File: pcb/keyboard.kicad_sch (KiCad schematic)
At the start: 50 parts, among them J1 TRRS, SW11 11, SW12 12, SW13 13, SW14 14, SW15 15, SW16 16, SW17 17, SW18 18, SW19 19, SW21 21, SW22 22, SW23 23, SW24 24, SW25 25, SW26 26, SW27 27, SW28 28, SW29 29, SW31 31, SW32 32, SW33 33, SW34 34, SW35 35, SW36 36, SW37 37, SW38 38, SW39 39, SW41 41, SW42 42, SW43 43, SW45 45, SW46 46, SW47 47, SW48 48, SW49 49, U1 EliteC

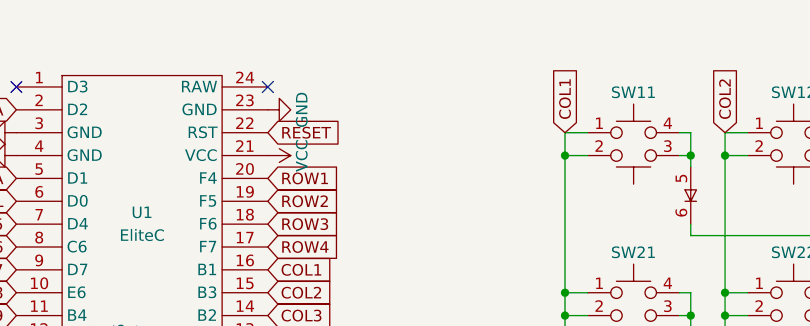
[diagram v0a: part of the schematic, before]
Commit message: add plate to 3D view
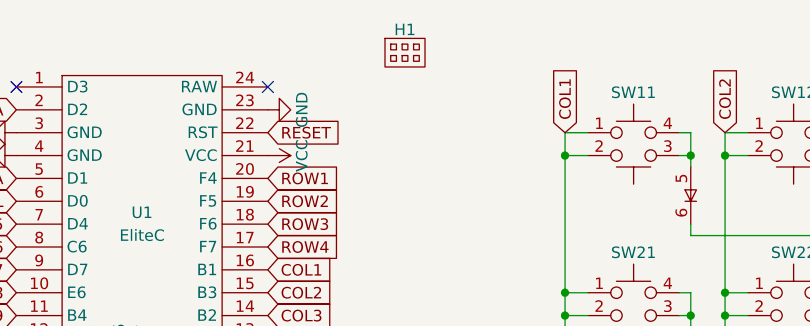
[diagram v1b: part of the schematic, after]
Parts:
- added H1: H1, Keyboard:RightPlate, symbol Keyboard:Plate
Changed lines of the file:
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@@
+    )
+  )
+  (symbol (lib_id "Keyboard:Plate") (at 85.09 30.48 0) (unit 1)
+    (in_bom yes) (on_board yes) (dnp no) (fields_autoplaced)
+    (property "Reference" "H1" (at 85.09 27.94 0) (do_not_autoplace)
+      (effects (font (size 1.27 1.27)))
+    )
+    (property "Value" "H1" (at 84.1375 30.1625 0) (do_not_autoplace)
+      (effects (font (size 1.27 1.27)) hide)
+    )
+    (property "Footprint" "Keyboard:RightPlate" (at 84.1375 30.1625 0)
+      (effects (font (size 1.27 1.27)) hide)
+    )
+    (property "Datasheet" "" (at 84.1375 30.1625 0)
+      (effects (font (size 1.27 1.27)) hide)
+    )
+    (instances
+      (project "keyboard"
+        (path "/7807834d-3d77-4d25-b9d8-d933072c7b84"
+          (reference "H1") (unit 1)
+        )
+      )
     )
   )

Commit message: move graphical copper arcs to traces; use default teardrop size
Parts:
- SW37, SW39: footprint Keyboard:Switch -> Keyboard:SwitchNo3D
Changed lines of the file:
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@@
       (effects (font (size 1.27 1.27)) hide)
     )
-    (property "Footprint" "Keyboard:Switch" (at 217.17 76.2 0)
+    (property "Footprint" "Keyboard:SwitchNo3D" (at 217.17 76.2 0)
       (effects (font (size 1.27 1.27)) hide)
     )
@@
       (effects (font (size 1.27 1.27)) hide)
     )
-    (property "Footprint" "Keyboard:Switch" (at 252.73 76.2 0)
-      (effects (font (size 1.27 1.27)) hide)
-    )
+    (property "Footprint" "Keyboard:SwitchNo3D" (at 252.73 76.2 0)
+      (effects (font (size 1.27 1.27)) hide)
+    )

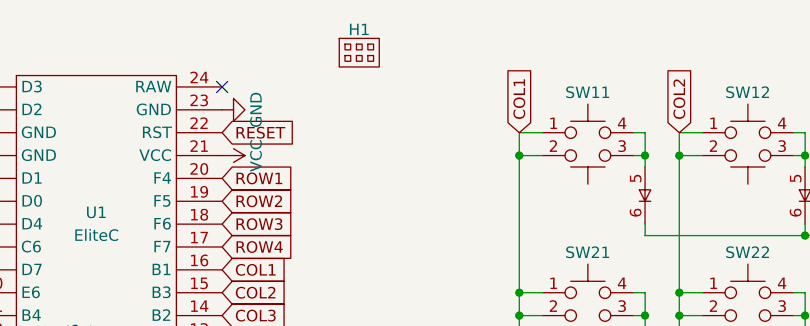
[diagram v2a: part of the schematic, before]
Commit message: support 3d view of left plate
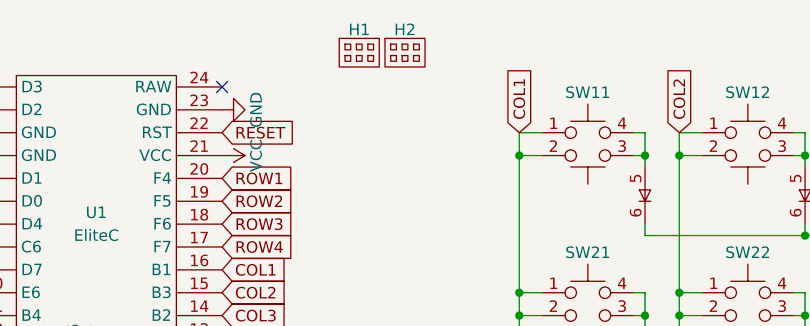
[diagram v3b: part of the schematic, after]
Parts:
- added H2: H1, Keyboard:LeftPlate, symbol Keyboard:Plate
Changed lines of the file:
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@@
+    )
+  )
+  (symbol (lib_id "Keyboard:Plate") (at 90.17 30.48 0) (unit 1)
+    (in_bom yes) (on_board yes) (dnp no) (fields_autoplaced)
+    (property "Reference" "H2" (at 90.17 27.94 0) (do_not_autoplace)
+      (effects (font (size 1.27 1.27)))
+    )
+    (property "Value" "H1" (at 89.2175 30.1625 0) (do_not_autoplace)
+      (effects (font (size 1.27 1.27)) hide)
+    )
+    (property "Footprint" "Keyboard:LeftPlate" (at 89.2175 30.1625 0)
+      (effects (font (size 1.27 1.27)) hide)
+    )
+    (property "Datasheet" "" (at 89.2175 30.1625 0)
+      (effects (font (size 1.27 1.27)) hide)
+    )
+    (instances
+      (project "keyboard"
+        (path "/7807834d-3d77-4d25-b9d8-d933072c7b84"
+          (reference "H2") (unit 1)
+        )
+      )
     )
   )

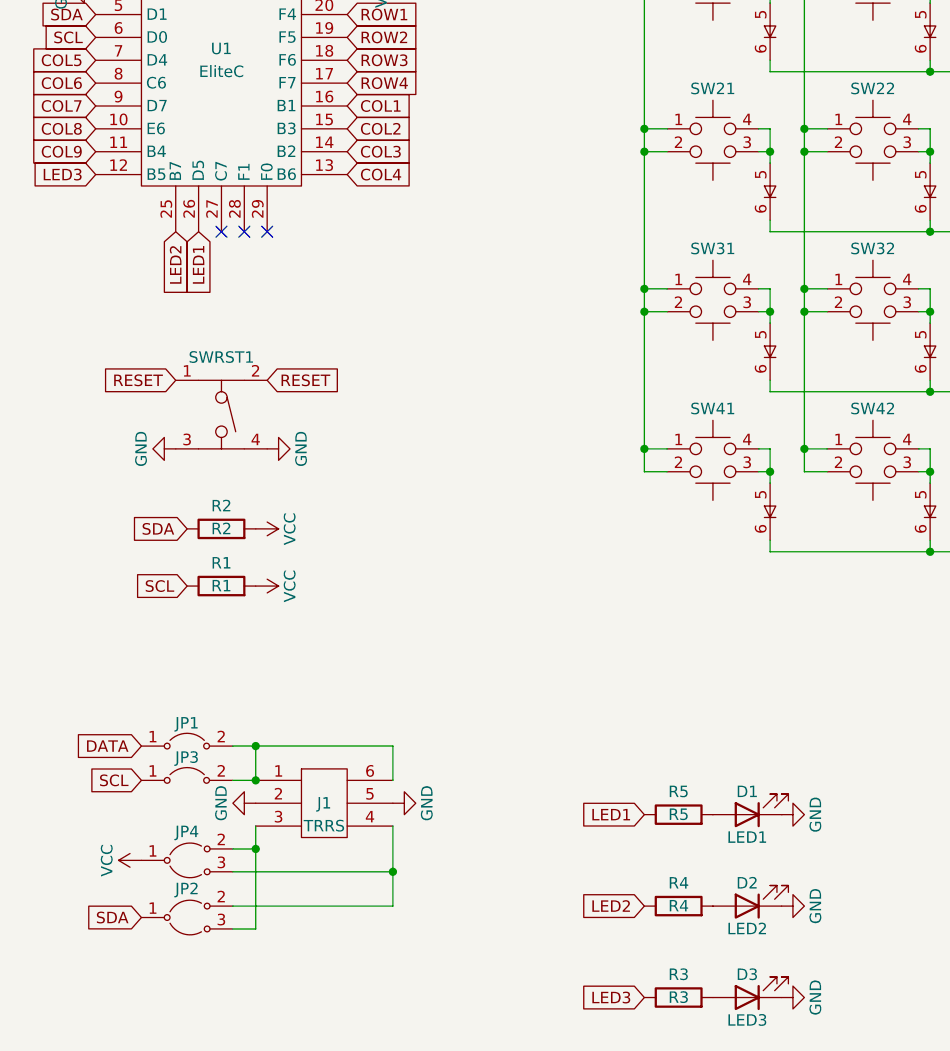
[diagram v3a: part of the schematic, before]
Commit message: hide back of LED by rotation; resistor after LED
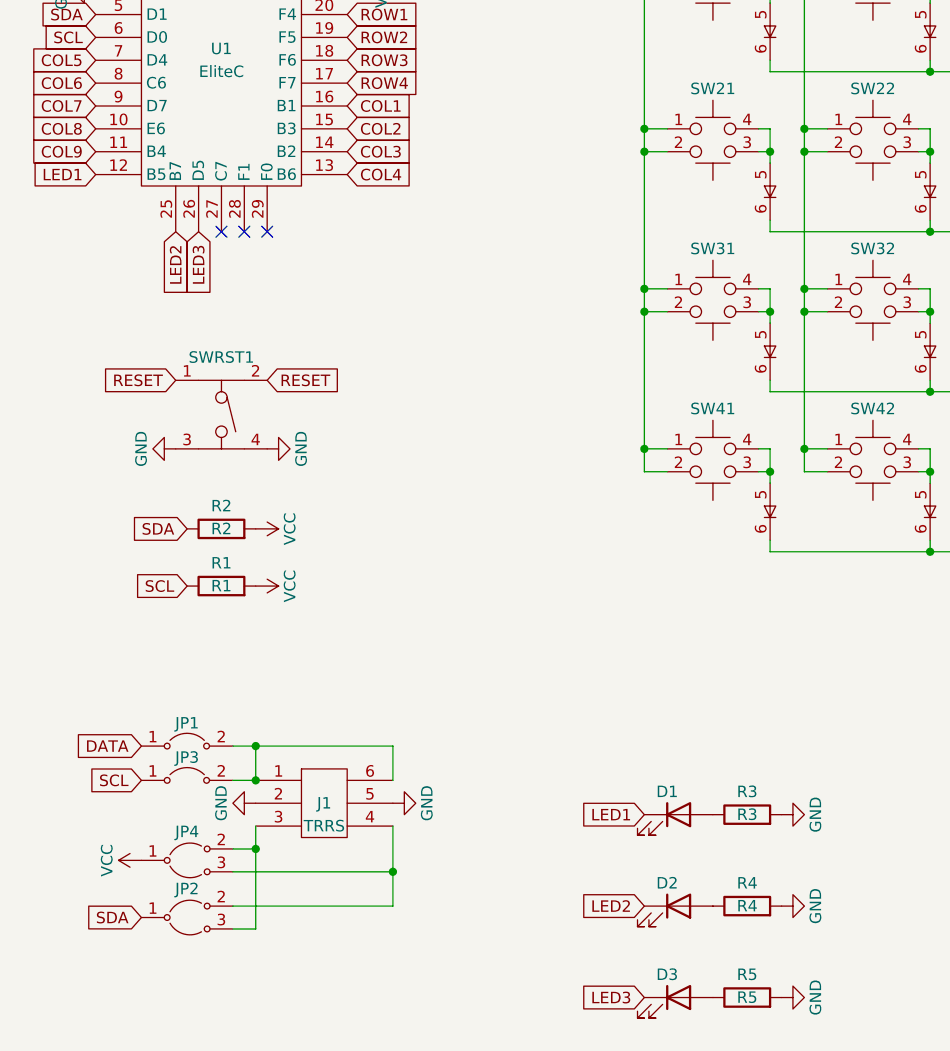
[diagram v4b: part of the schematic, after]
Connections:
- net GND: now also R3.2, R4.2, R5.2; no longer D1.1 (K), D2.1 (K), D3.1 (K)
- net LED1: now also D1.1 (K), U1.12 (B5); no longer R5.1, U1.26 (D5)
- net LED2: now also D2.1 (K); no longer R4.1
- net LED3: now also D3.1 (K), U1.26 (D5); no longer R3.1, U1.12 (B5)
- net at D3.2 (A): now also R5.1; no longer R3.2
- net at D1.2 (A): now also R3.1; no longer R5.2
- net at D2.2 (A): now also R4.1; no longer R4.2

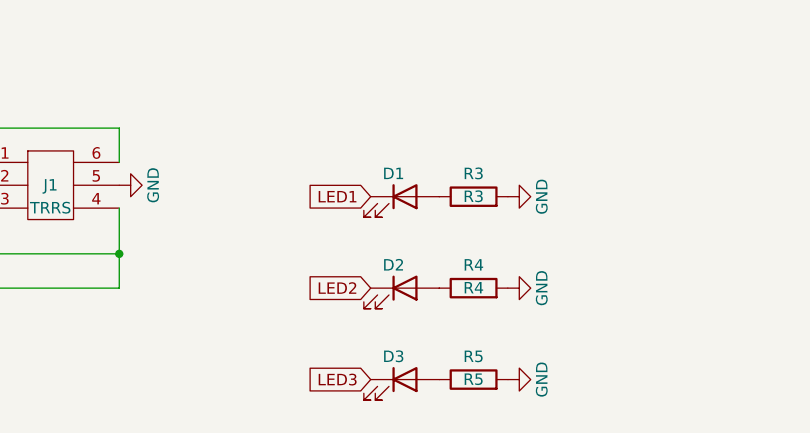
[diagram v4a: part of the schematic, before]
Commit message: fix schematic of LED pins
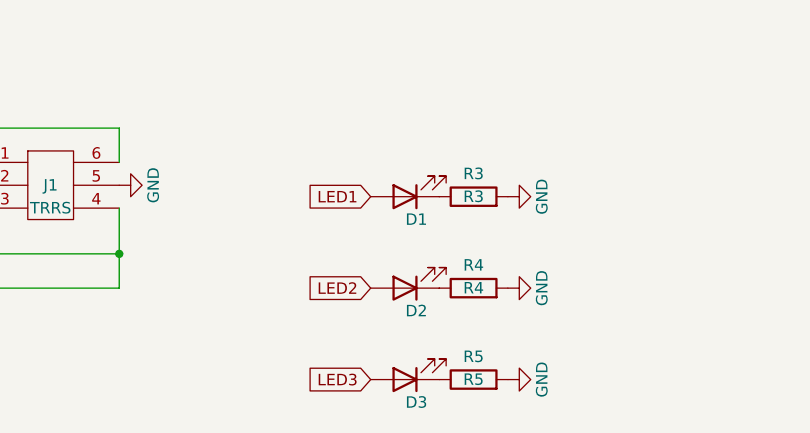
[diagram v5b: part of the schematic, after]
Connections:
- net LED1: now also D1.2 (A); no longer D1.1 (K)
- net LED2: now also D2.2 (A); no longer D2.1 (K)
- net LED3: now also D3.2 (A); no longer D3.1 (K)
- net at R5.1: now also D3.1 (K); no longer D3.2 (A)
- net at R4.1: now also D2.1 (K); no longer D2.2 (A)
- net at R3.1: now also D1.1 (K); no longer D1.2 (A)
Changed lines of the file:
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@@
-    )
-  )
-  (symbol (lib_id "Device:LED") (at 106.68 153.67 0) (unit 1)
-    (in_bom yes) (on_board yes) (dnp no)
-    (property "Reference" "D3" (at 105.41 151.13 0)
-      (effects (font (size 1.27 1.27)))
-    )
-    (property "Value" "LED3" (at 105.0925 149.86 0)
-      (effects (font (size 1.27 1.27)) hide)
-    )
-    (property "Footprint" "Keyboard:LED" (at 106.68 153.67 0)
-      (effects (font (size 1.27 1.27)) hide)
-    )
-    (property "Datasheet" "~" (at 106.68 153.67 0)
-      (effects (font (size 1.27 1.27)) hide)
-    )
-    (pin "1")
-    (pin "2")
-    (instances
-      (project "keyboard"
-        (path "/7807834d-3d77-4d25-b9d8-d933072c7b84"
-          (reference "D3") (unit 1)
-        )
-      )
     )
   )
@@
     )
   )
-  (symbol (lib_id "Device:LED") (at 106.68 143.51 0) (unit 1)
-    (in_bom yes) (on_board yes) (dnp no)
-    (property "Reference" "D2" (at 105.41 140.97 0)
-      (effects (font (size 1.27 1.27)))
-    )
-    (property "Value" "LED2" (at 105.0925 139.7 0)
-      (effects (font (size 1.27 1.27)) hide)
-    )
-    (property "Footprint" "Keyboard:LED" (at 106.68 143.51 0)
-      (effects (font (size 1.27 1.27)) hide)
-    )
-    (property "Datasheet" "~" (at 106.68 143.51 0)
-      (effects (font (size 1.27 1.27)) hide)
-    )
-    (pin "1")
-    (pin "2")
-    (instances
-      (project "keyboard"
-        (path "/7807834d-3d77-4d25-b9d8-d933072c7b84"
-          (reference "D2") (unit 1)
-        )
-      )
-    )
-  )
   (symbol (lib_id "Keyboard:Switch") (at 163.83 76.2 0) (unit 1)
     (in_bom yes) (on_board yes) (dnp no) (fields_autoplaced)
@@
     )
   )
+  (symbol (lib_id "Device:LED") (at 106.68 143.51 180) (unit 1)
+    (in_bom yes) (on_board yes) (dnp no)
+    (property "Reference" "D2" (at 107.95 146.05 0)
+      (effects (font (size 1.27 1.27)))
+    )
+    (property "Value" "LED2" (at 108.2675 147.32 0)
+      (effects (font (size 1.27 1.27)) hide)
+    )
+    (property "Footprint" "Keyboard:LED" (at 106.68 143.51 0)
+      (effects (font (size 1.27 1.27)) hide)
+    )
+    (property "Datasheet" "~" (at 106.68 143.51 0)
+      (effects (font (size 1.27 1.27)) hide)
+    )
+    (pin "1")
+    (pin "2")
+    (instances
+      (project "keyboard"
+        (path "/7807834d-3d77-4d25-b9d8-d933072c7b84"
+          (reference "D2") (unit 1)
+        )
+      )
+    )
+  )
   (symbol (lib_id "Keyboard:Switch") (at 217.17 40.64 0) (unit 1)
     (in_bom yes) (on_board yes) (dnp no) (fields_autoplaced)
@@
     )
   )
+  (symbol (lib_id "Device:LED") (at 106.68 153.67 180) (unit 1)
+    (in_bom yes) (on_board yes) (dnp no)
+    (property "Reference" "D3" (at 107.95 156.21 0)
+      (effects (font (size 1.27 1.27)))
+    )
+    (property "Value" "LED3" (at 108.2675 157.48 0)
+      (effects (font (size 1.27 1.27)) hide)
+    )
+    (property "Footprint" "Keyboard:LED" (at 106.68 153.67 0)
+      (effects (font (size 1.27 1.27)) hide)
+    )
+    (property "Datasheet" "~" (at 106.68 153.67 0)
+      (effects (font (size 1.27 1.27)) hide)
+    )
+    (pin "1")
+    (pin "2")
+    (instances
+      (project "keyboard"
+        (path "/7807834d-3d77-4d25-b9d8-d933072c7b84"
+          (reference "D3") (unit 1)
+        )
+      )
+    )
+  )
   (symbol (lib_id "power:VCC") (at 69.85 41.91 270) (unit 1)
     (in_bom yes) (on_board yes) (dnp no) (fields_autoplaced)
@@
     )
   )
+  (symbol (lib_id "Device:LED") (at 106.68 133.35 180) (unit 1)
+    (in_bom yes) (on_board yes) (dnp no)
+    (property "Reference" "D1" (at 107.95 135.89 0)
+      (effects (font (size 1.27 1.27)))
+    )
+    (property "Value" "LED1" (at 108.2675 137.16 0)
+      (effects (font (size 1.27 1.27)) hide)
+    )
+    (property "Footprint" "Keyboard:LED" (at 106.68 133.35 0)
+      (effects (font (size 1.27 1.27)) hide)
+    )
+    (property "Datasheet" "~" (at 106.68 133.35 0)
+      (effects (font (size 1.27 1.27)) hide)
+    )
+    (pin "1")
+    (pin "2")
+    (instances
+      (project "keyboard"
+        (path "/7807834d-3d77-4d25-b9d8-d933072c7b84"
+          (reference "D1") (unit 1)
+        )
+      )
+    )
+  )
   (symbol (lib_id "Keyboard:Switch") (at 181.61 76.2 0) (unit 1)
     (in_bom yes) (on_board yes) (dnp no) (fields_autoplaced)
@@
         )
       )
-    )
-  )
-  (symbol (lib_id "Device:LED") (at 106.68 133.35 0) (unit 1)
-    (in_bom yes) (on_board yes) (dnp no)
-    (property "Reference" "D1" (at 105.41 130.81 0)
-      (effects (font (size 1.27 1.27)))
-    )
-    (property "Value" "LED1" (at 105.0925 129.54 0)
-      (effects (font (size 1.27 1.27)) hide)
-    )
-    (property "Footprint" "Keyboard:LED" (at 106.68 133.35 0)
-      (effects (font (size 1.27 1.27)) hide)
-    )
-    (property "Datasheet" "~" (at 106.68 133.35 0)
-      (effects (font (size 1.27 1.27)) hide)
-    )
-    (pin "1")
-    (pin "2")
-    (instances
-      (project "keyboard"
-        (path "/7807834d-3d77-4d25-b9d8-d933072c7b84"
-          (reference "D1") (unit 1)
-        )
-      )

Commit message: improve switch double pads
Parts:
- SW16, SW26, SW35, SW36, SW45, SW46: footprint Keyboard:Switch -> Keyboard:SwitchDouble
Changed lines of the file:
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@@
       (effects (font (size 1.27 1.27)) hide)
     )
-    (property "Footprint" "Keyboard:Switch" (at 199.39 76.2 0)
+    (property "Footprint" "Keyboard:SwitchDouble" (at 199.39 76.2 0)
       (effects (font (size 1.27 1.27)) hide)
     )
@@
       (effects (font (size 1.27 1.27)) hide)
     )
-    (property "Footprint" "Keyboard:Switch" (at 199.39 58.42 0)
+    (property "Footprint" "Keyboard:SwitchDouble" (at 199.39 58.42 0)
       (effects (font (size 1.27 1.27)) hide)
     )
@@
       (effects (font (size 1.27 1.27)) hide)
     )
-    (property "Footprint" "Keyboard:Switch" (at 181.61 93.98 0)
+    (property "Footprint" "Keyboard:SwitchDouble" (at 181.61 93.98 0)
       (effects (font (size 1.27 1.27)) hide)
     )
@@
       (effects (font (size 1.27 1.27)) hide)
     )
-    (property "Footprint" "Keyboard:Switch" (at 181.61 76.2 0)
+    (property "Footprint" "Keyboard:SwitchDouble" (at 181.61 76.2 0)
       (effects (font (size 1.27 1.27)) hide)
     )
@@
       (effects (font (size 1.27 1.27)) hide)
     )
-    (property "Footprint" "Keyboard:Switch" (at 199.39 40.64 0)
+    (property "Footprint" "Keyboard:SwitchDouble" (at 199.39 40.64 0)
       (effects (font (size 1.27 1.27)) hide)
     )
@@
       (effects (font (size 1.27 1.27)) hide)
     )
-    (property "Footprint" "Keyboard:Switch" (at 199.39 93.98 0)
-      (effects (font (size 1.27 1.27)) hide)
-    )
+    (property "Footprint" "Keyboard:SwitchDouble" (at 199.39 93.98 0)
+      (effects (font (size 1.27 1.27)) hide)
+    )
